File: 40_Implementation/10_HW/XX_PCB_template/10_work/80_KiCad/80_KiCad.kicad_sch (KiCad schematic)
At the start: 41 parts, among them J1 Power, J2 Digital/PWM, J3 Analog, J4 Digital/PWM, J5 Conn_01x03_Socket, SW1 SW_SPST, U1 OPA340P, U2 OPA340P

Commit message: v1.1.1
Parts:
- renumbered A_In1_N to A_In1_N1, A_In2_N to A_In2_N1, A_In_P to A_In_P1
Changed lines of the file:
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@@
 		(on_board yes)
 		(dnp no)
-		(property "Reference" "A_In2_N"
+		(property "Reference" "A_In2_N1"
 			(at 192.024 73.406 0)
 			(effects
@@
 			(project "80_KiCad"
 				(path "/e63e39d7-6ac0-4ffd-8aa3-1841a4541b55"
-					(reference "A_In2_N")
+					(reference "A_In2_N1")
 					(unit 1)
 				)
@@
 		(dnp no)
 		(fields_autoplaced yes)
-		(property "Reference" "A_In1_N"
+		(property "Reference" "A_In1_N1"
 			(at 119.38 65.2779 0)
 			(effects
@@
 			(project "80_KiCad"
 				(path "/e63e39d7-6ac0-4ffd-8aa3-1841a4541b55"
-					(reference "A_In1_N")
+					(reference "A_In1_N1")
 					(unit 1)
 				)
@@
 		(dnp no)
 		(fields_autoplaced yes)
-		(property "Reference" "A_In_P"
+		(property "Reference" "A_In_P1"
 			(at 133.35 34.7979 0)
 			(effects
@@
 			(project "80_KiCad"
 				(path "/e63e39d7-6ac0-4ffd-8aa3-1841a4541b55"
-					(reference "A_In_P")
-					(unit 1)
-				)
+					(reference "A_In_P1")
+					(unit 1)
+				)

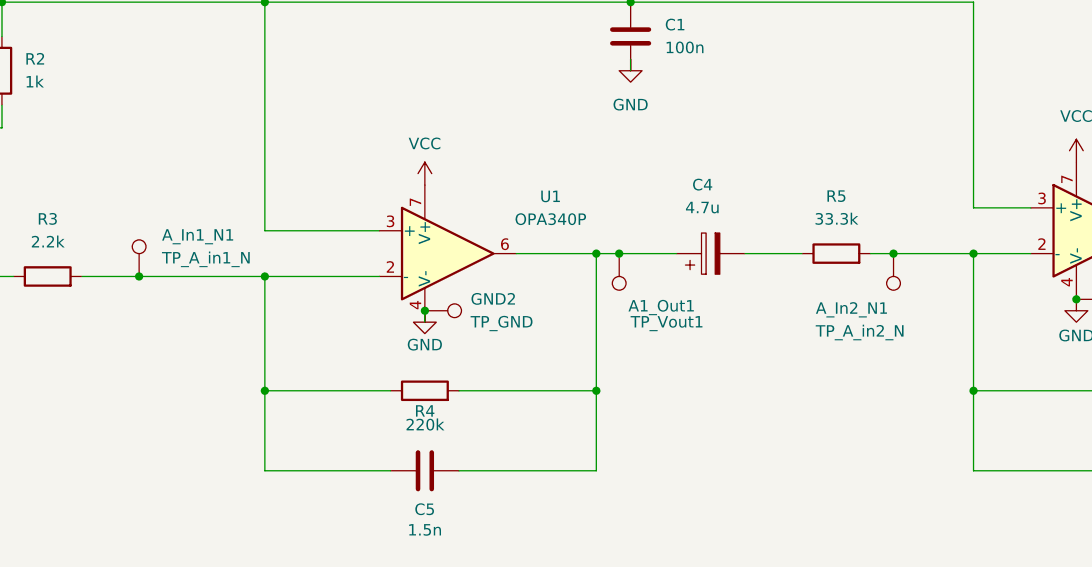
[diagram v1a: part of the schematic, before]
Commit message: Changed References - Silk Layer - Minor Changes
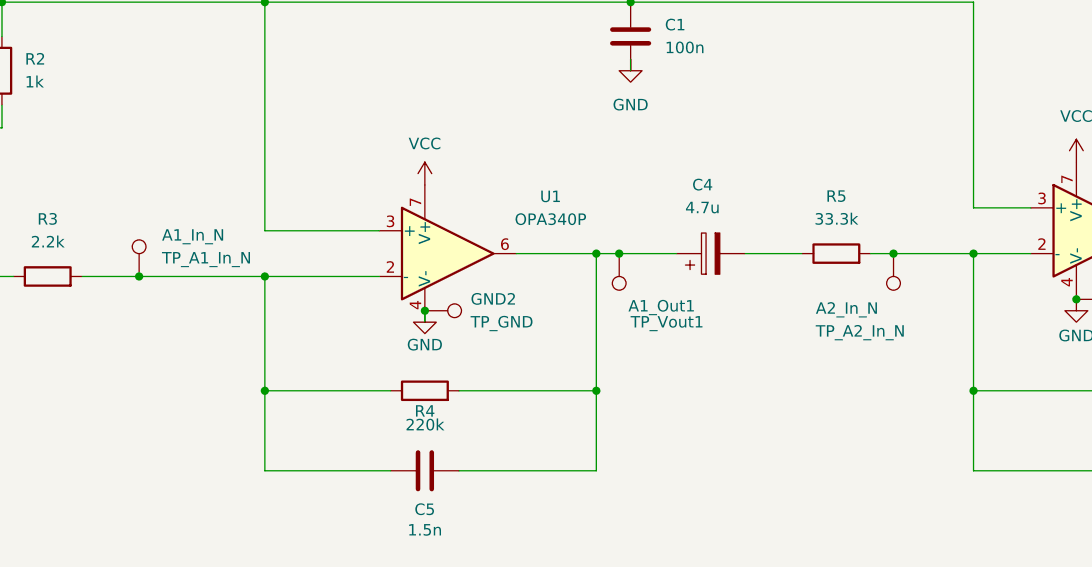
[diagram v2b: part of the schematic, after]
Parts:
- A1_In_N: renamed from A_In1_N1; value TP_A_in1_N -> TP_A1_In_N
- A2_In_N: renamed from A_In2_N1; value TP_A_in2_N -> TP_A2_In_N
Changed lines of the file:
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@@
 		(on_board yes)
 		(dnp no)
-		(property "Reference" "A_In2_N1"
+		(property "Reference" "A2_In_N"
 			(at 192.024 73.406 0)
 			(effects
@@
 			)
 		)
-		(property "Value" "TP_A_in2_N"
+		(property "Value" "TP_A2_In_N"
 			(at 192.024 75.946 0)
 			(effects
@@
 			(project "80_KiCad"
 				(path "/e63e39d7-6ac0-4ffd-8aa3-1841a4541b55"
-					(reference "A_In2_N1")
+					(reference "A2_In_N")
 					(unit 1)
 				)
@@
 		(dnp no)
 		(fields_autoplaced yes)
-		(property "Reference" "A_In1_N1"
+		(property "Reference" "A1_In_N"
 			(at 119.38 65.2779 0)
 			(effects
@@
 			)
 		)
-		(property "Value" "TP_A_in1_N"
+		(property "Value" "TP_A1_In_N"
 			(at 119.38 67.8179 0)
 			(effects
@@
 			(project "80_KiCad"
 				(path "/e63e39d7-6ac0-4ffd-8aa3-1841a4541b55"
-					(reference "A_In1_N1")
+					(reference "A1_In_N")
 					(unit 1)
 				)

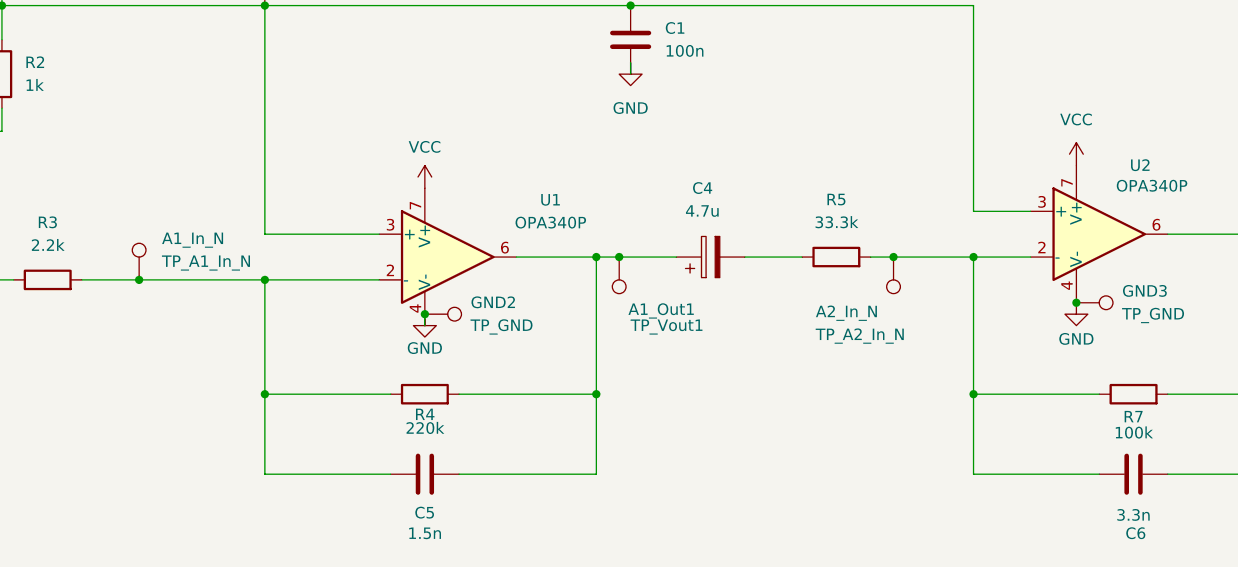
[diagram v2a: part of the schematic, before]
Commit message: After capacitor change - 21.05s
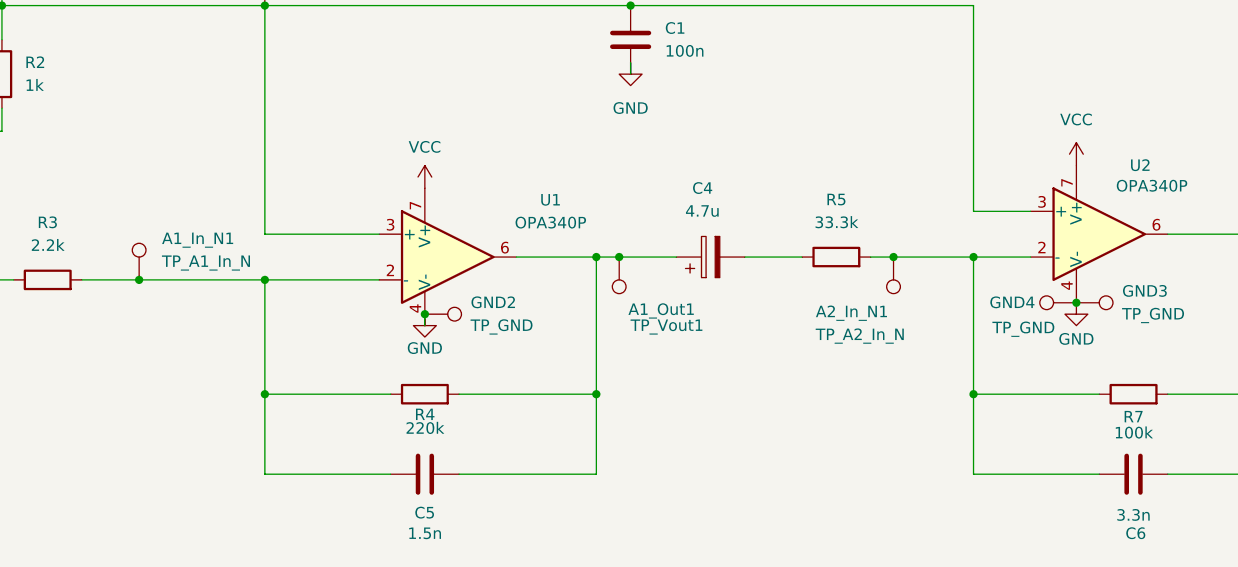
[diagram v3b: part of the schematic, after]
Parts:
- added GND4: TP_GND, Connector_PinHeader_2.54mm:PinHeader_1x01_P2.54mm_Vertical, symbol Connector:TestPoint
- C1: footprint Capacitor_THT:C_Rect_L7.2mm_W3.0mm_P5.00mm_FKS2_FKP2_MKS2_MKP2 -> Capacitor_THT:C_Rect_L7.2mm_W2.5mm_P5.00mm_FKS2_FKP2_MKS2_MKP2
- C2: footprint Capacitor_THT:CP_Radial_D10.0mm_P2.50mm -> Capacitor_THT:CP_Radial_D5.0mm_P2.00mm
- C3, C4: footprint Capacitor_THT:CP_Radial_D10.0mm_P2.50mm -> Capacitor_THT:CP_Radial_D5.0mm_P2.50mm
- C5, C6: footprint Capacitor_THT:C_Rect_L7.2mm_W3.0mm_P5.00mm_FKS2_FKP2_MKS2_MKP2 -> Capacitor_THT:C_Rect_L7.2mm_W7.2mm_P5.00mm_FKS2_FKP2_MKS2_MKP2
- R1, R10, R11, R12, R2, R3, R4, R5, R6, R7, R8, R9: footprint Resistor_THT:R_Axial_DIN0207_L6.3mm_D2.5mm_P7.62mm_Horizontal -> Resistor_THT:R_Axial_DIN0207_L6.3mm_D2.5mm_P10.16mm_Horizontal
- SW1: footprint Button_Switch_THT:SW_PUSH_6mm -> Button_Switch_THT:SW_PUSH_6mm_H7.3mm
- renumbered A1_In_N to A1_In_N1, A2_In_N to A2_In_N1
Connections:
- net GND: now also GND4.1
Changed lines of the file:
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@@
 			)
 		)
-		(property "Footprint" "Resistor_THT:R_Axial_DIN0207_L6.3mm_D2.5mm_P7.62mm_Horizontal"
+		(property "Footprint" "Resistor_THT:R_Axial_DIN0207_L6.3mm_D2.5mm_P10.16mm_Horizontal"
 			(at 48.26 47.498 90)
 			(effects
@@
 			)
 		)
-		(property "Footprint" "Capacitor_THT:C_Rect_L7.2mm_W3.0mm_P5.00mm_FKS2_FKP2_MKS2_MKP2"
+		(property "Footprint" "Capacitor_THT:C_Rect_L7.2mm_W7.2mm_P5.00mm_FKS2_FKP2_MKS2_MKP2"
 			(at 152.4 90.4748 0)
 			(effects
@@
 			)
 		)
-		(property "Footprint" "Resistor_THT:R_Axial_DIN0207_L6.3mm_D2.5mm_P7.62mm_Horizontal"
+		(property "Footprint" "Resistor_THT:R_Axial_DIN0207_L6.3mm_D2.5mm_P10.16mm_Horizontal"
 			(at 141.478 121.92 90)
 			(effects
@@
 			)
 		)
-		(property "Footprint" "Resistor_THT:R_Axial_DIN0207_L6.3mm_D2.5mm_P7.62mm_Horizontal"
+		(property "Footprint" "Resistor_THT:R_Axial_DIN0207_L6.3mm_D2.5mm_P10.16mm_Horizontal"
 			(at 194.31 69.088 90)
 			(effects
@@
 			)
 		)
-		(property "Footprint" "Resistor_THT:R_Axial_DIN0207_L6.3mm_D2.5mm_P7.62mm_Horizontal"
+		(property "Footprint" "Resistor_THT:R_Axial_DIN0207_L6.3mm_D2.5mm_P10.16mm_Horizontal"
 			(at 152.4 137.668 90)
 			(effects
@@
 			)
 		)
-		(property "Footprint" "Resistor_THT:R_Axial_DIN0207_L6.3mm_D2.5mm_P7.62mm_Horizontal"
+		(property "Footprint" "Resistor_THT:R_Axial_DIN0207_L6.3mm_D2.5mm_P10.16mm_Horizontal"
 			(at 152.4 151.892 90)
 			(effects
@@
 			)
 		)
-		(property "Footprint" "Resistor_THT:R_Axial_DIN0207_L6.3mm_D2.5mm_P7.62mm_Horizontal"
+		(property "Footprint" "Resistor_THT:R_Axial_DIN0207_L6.3mm_D2.5mm_P10.16mm_Horizontal"
 			(at 106.68 71.628 90)
 			(effects
@@
 			)
 		)
-		(property "Footprint" "Button_Switch_THT:SW_PUSH_6mm"
+		(property "Footprint" "Button_Switch_THT:SW_PUSH_6mm_H7.3mm"
 			(at 156.21 125.73 0)
 			(effects
@@
 			)
 		)
-		(property "Footprint" "Resistor_THT:R_Axial_DIN0207_L6.3mm_D2.5mm_P7.62mm_Horizontal"
+		(property "Footprint" "Resistor_THT:R_Axial_DIN0207_L6.3mm_D2.5mm_P10.16mm_Horizontal"
 			(at 254 66.548 90)
 			(effects
@@
 			)
 		)
-		(property "Footprint" "Resistor_THT:R_Axial_DIN0207_L6.3mm_D2.5mm_P7.62mm_Horizontal"
+		(property "Footprint" "Resistor_THT:R_Axial_DIN0207_L6.3mm_D2.5mm_P10.16mm_Horizontal"
 			(at 152.4 143.002 90)
 			(effects
@@
 		(on_board yes)
 		(dnp no)
-		(fields_autoplaced yes)
 		(property "Reference" "U1"
 			(at 162.56 60.9914 0)
@@
 			)
 		)
-		(property "Footprint" "Resistor_THT:R_Axial_DIN0207_L6.3mm_D2.5mm_P7.62mm_Horizontal"
+		(property "Footprint" "Resistor_THT:R_Axial_DIN0207_L6.3mm_D2.5mm_P10.16mm_Horizontal"
 			(at 99.822 34.29 90)
 			(effects
@@
 			)
 		)
-		(property "Footprint" "Capacitor_THT:CP_Radial_D10.0mm_P2.50mm"
+		(property "Footprint" "Capacitor_THT:CP_Radial_D5.0mm_P2.50mm"
 			(at 184.15 66.3448 0)
 			(effects
@@
 	)
 	(symbol
+		(lib_id "Connector:TestPoint")
+		(at 220.98 72.39 90)
+		(unit 1)
+		(exclude_from_sim no)
+		(in_bom yes)
+		(on_board yes)
+		(dnp no)
+		(property "Reference" "GND4"
+			(at 213.868 72.39 90)
+			(effects
+				(font
+					(size 1.27 1.27)
+				)
+			)
+		)
+		(property "Value" "TP_GND"
+			(at 215.138 75.184 90)
+			(effects
+				(font
+					(size 1.27 1.27)
+				)
+			)
+		)
+		(property "Footprint" "Connector_PinHeader_2.54mm:PinHeader_1x01_P2.54mm_Vertical"
+			(at 220.98 67.31 0)
+			(effects
+				(font
+					(size 1.27 1.27)
+				)
+				(hide yes)
+			)
+		)
+		(property "Datasheet" "~"
+			(at 220.98 67.31 0)
+			(effects
+				(font
+					(size 1.27 1.27)
+				)
+				(hide yes)
+			)
+		)
+		(property "Description" "test point"
+			(at 220.98 72.39 0)
+			(effects
+				(font
+					(size 1.27 1.27)
+				)
+				(hide yes)
+			)
+		)
+		(pin "1"
+		)
+		(instances
+			(project "80_KiCad"
+				(path "/e63e39d7-6ac0-4ffd-8aa3-1841a4541b55"
+					(reference "GND4")
+					(unit 1)
+				)
+			)
+		)
+	)
+	(symbol
 		(lib_id "power:PWR_FLAG")
 		(at 34.29 135.89 90)
@@
 			)
 		)
-		(property "Footprint" "Resistor_THT:R_Axial_DIN0207_L6.3mm_D2.5mm_P7.62mm_Horizontal"
+		(property "Footprint" "Resistor_THT:R_Axial_DIN0207_L6.3mm_D2.5mm_P10.16mm_Horizontal"
 			(at 227.33 84.328 90)
 			(effects
@@
 			)
 		)
-		(property "Footprint" "Resistor_THT:R_Axial_DIN0207_L6.3mm_D2.5mm_P7.62mm_Horizontal"
+		(property "Footprint" "Resistor_THT:R_Axial_DIN0207_L6.3mm_D2.5mm_P10.16mm_Horizontal"
 			(at 99.822 46.99 90)
 			(effects
@@
 		(on_board yes)
 		(dnp no)
-		(property "Reference" "A2_In_N"
+		(property "Reference" "A2_In_N1"
 			(at 192.024 73.406 0)
 			(effects
@@
 			(project "80_KiCad"
 				(path "/e63e39d7-6ac0-4ffd-8aa3-1841a4541b55"
-					(reference "A2_In_N")
+					(reference "A2_In_N1")
 					(unit 1)
 				)
@@
 		(dnp no)
 		(fields_autoplaced yes)
-		(property "Reference" "A1_In_N"
+		(property "Reference" "A1_In_N1"
 			(at 119.38 65.2779 0)
 			(effects
@@
 			(project "80_KiCad"
 				(path "/e63e39d7-6ac0-4ffd-8aa3-1841a4541b55"
-					(reference "A1_In_N")
+					(reference "A1_In_N1")
 					(unit 1)
 				)
@@
 			)
 		)
-		(property "Footprint" "Capacitor_THT:C_Rect_L7.2mm_W3.0mm_P5.00mm_FKS2_FKP2_MKS2_MKP2"
+		(property "Footprint" "Capacitor_THT:C_Rect_L7.2mm_W2.5mm_P5.00mm_FKS2_FKP2_MKS2_MKP2"
 			(at 172.4152 46.99 0)
 			(effects
@@
 			)
 		)
-		(property "Footprint" "Capacitor_THT:C_Rect_L7.2mm_W3.0mm_P5.00mm_FKS2_FKP2_MKS2_MKP2"
+		(property "Footprint" "Capacitor_THT:C_Rect_L7.2mm_W7.2mm_P5.00mm_FKS2_FKP2_MKS2_MKP2"
 			(at 231.14 90.4748 0)
 			(effects
@@
 			)
 		)
-		(property "Footprint" "Capacitor_THT:CP_Radial_D10.0mm_P2.50mm"
+		(property "Footprint" "Capacitor_THT:CP_Radial_D5.0mm_P2.00mm"
 			(at 92.4052 49.53 0)
 			(effects
@@
 			)
 		)
-		(property "Footprint" "Resistor_THT:R_Axial_DIN0207_L6.3mm_D2.5mm_P7.62mm_Horizontal"
+		(property "Footprint" "Resistor_THT:R_Axial_DIN0207_L6.3mm_D2.5mm_P10.16mm_Horizontal"
 			(at 148.59 84.328 90)
 			(effects
@@
 			)
 		)
-		(property "Footprint" "Capacitor_THT:CP_Radial_D10.0mm_P2.50mm"
+		(property "Footprint" "Capacitor_THT:CP_Radial_D5.0mm_P2.50mm"
 			(at 87.63 70.8152 0)
 			(effects

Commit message: Almost Submitted
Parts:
- R6: value 100 -> 100k
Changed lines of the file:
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@@
 			)
 		)
-		(property "Value" "100"
+		(property "Value" "100k"
 			(at 254 60.96 90)
 			(effects
